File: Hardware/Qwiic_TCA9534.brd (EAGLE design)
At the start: 30.5 x 25.4 mm, 24 parts, among them J2 SMD, J3 PTH, J4 SMD

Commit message: partial route
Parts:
- removed J8: (no value), SparkFun-Connectors:1X10_NO_SILK
- added J5: (no value), SparkFun-Connectors:1X08_NO_SILK
- moved R5 19.8 mm to (6.86, 5.08), turned to 0 degrees
- moved JP7 11.7 mm to (11.4, 6.35)
- moved JP5 7.62 mm to (15.2, 6.35)
- moved JP1 4.58 mm to (19.1, 6.35)
- moved R3 3.30 mm to (23.6, 5.08)
- moved R1 3.05 mm to (23.6, 7.62)
- moved C4 0.52 mm to (6.86, 7.49)
- moved R2 0.51 mm to (12.7, 19.8)
- moved R4 0.51 mm to (17.8, 19.8)
- moved SJ5 0.38 mm to (15.2, 19.9)
- moved U$2 0.28 mm to (26.2, 20.3)
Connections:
- removed net 2: J8.3, U$3.5
- removed net SCL/SCK/RX: J2.4, J3.4, J4.4
- removed net SDA/MISO/TX: J2.3, J3.3, J4.3
- new net P1: J5.2, U$3.5
- net GND: no longer J8.1, J8.10
- net P0: now also J5.1; no longer J8.2
- net P2: now also J5.3; no longer J8.4
- net P3: now also J5.4; no longer J8.5
- net P4: now also J5.5; no longer J8.6
- net P5: now also J5.6; no longer J8.7
- net P6: now also J5.7; no longer J8.8
- net P7: now also J5.8; no longer J8.9
- net SCL: now also J2.4, J3.4, J4.4, R4.1
- net SDA: now also J2.3, J3.3, J4.3, R2.1
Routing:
- net 3.3V: track 0.00 -> 27.0 mm
- net SCL: track 0.00 -> 20.8 mm, vias 0 -> 2
- net SDA: track 0.00 -> 18.4 mm
- net !INT: track 0.00 -> 16.4 mm
- net P0: track 0.00 -> 15.5 mm
- net P1: track 0.00 -> 14.2 mm
- net P7: track 0.00 -> 13.2 mm
- net P2: track 0.00 -> 13.0 mm
- net P6: track 0.00 -> 11.9 mm
- net P3: track 0.00 -> 11.7 mm
- net P5: track 0.00 -> 10.6 mm
- net P4: track 0.00 -> 8.39 mm
- net A1: track 0.00 -> 6.58 mm
- net A2: track 0.00 -> 4.99 mm
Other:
- board text added: "Qwiic GPIO"

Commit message: route complete
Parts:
- moved R2 0.25 mm to (12.7, 19.6), turned to 90 degrees
- moved R4 0.25 mm to (17.8, 19.6), turned to 90 degrees
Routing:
- net 3.3V: track 27.0 -> 72.3 mm, vias 0 -> 4
- net A0: track 0.00 -> 33.9 mm, vias 0 -> 2
- net SDA: track 18.4 -> 46.6 mm, vias 0 -> 4
- net SCL: track 20.8 -> 43.3 mm, vias 2 -> 5
- net A1: track 6.58 -> 14.7 mm, vias 0 -> 1
- net SCL_PU1: track 0.00 -> 7.50 mm, vias 0 -> 1
- net SDA_PU1: track 0.00 -> 7.34 mm, vias 0 -> 1
- net A2: track 4.99 -> 10.0 mm, vias 0 -> 1
- net GND: track 0.00 -> 2.70 mm, vias 0 -> 2
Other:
- board text removed: "TCA9534"

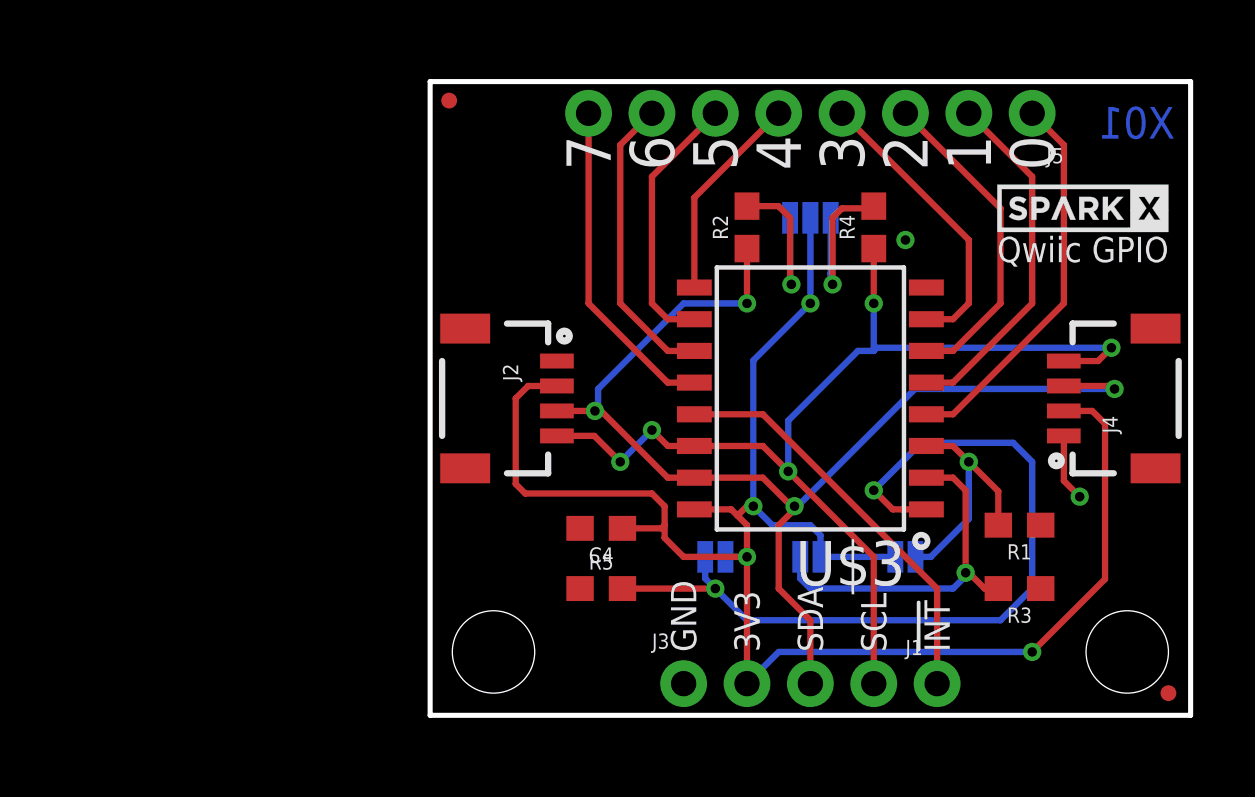
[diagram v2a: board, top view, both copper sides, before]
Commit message: starting to build out example 1
example 1 is to set a pin on the expander as output or input, then set it as high or low. currently the setPinMode() function works, next is to make a 'digitalWrite' equivalent
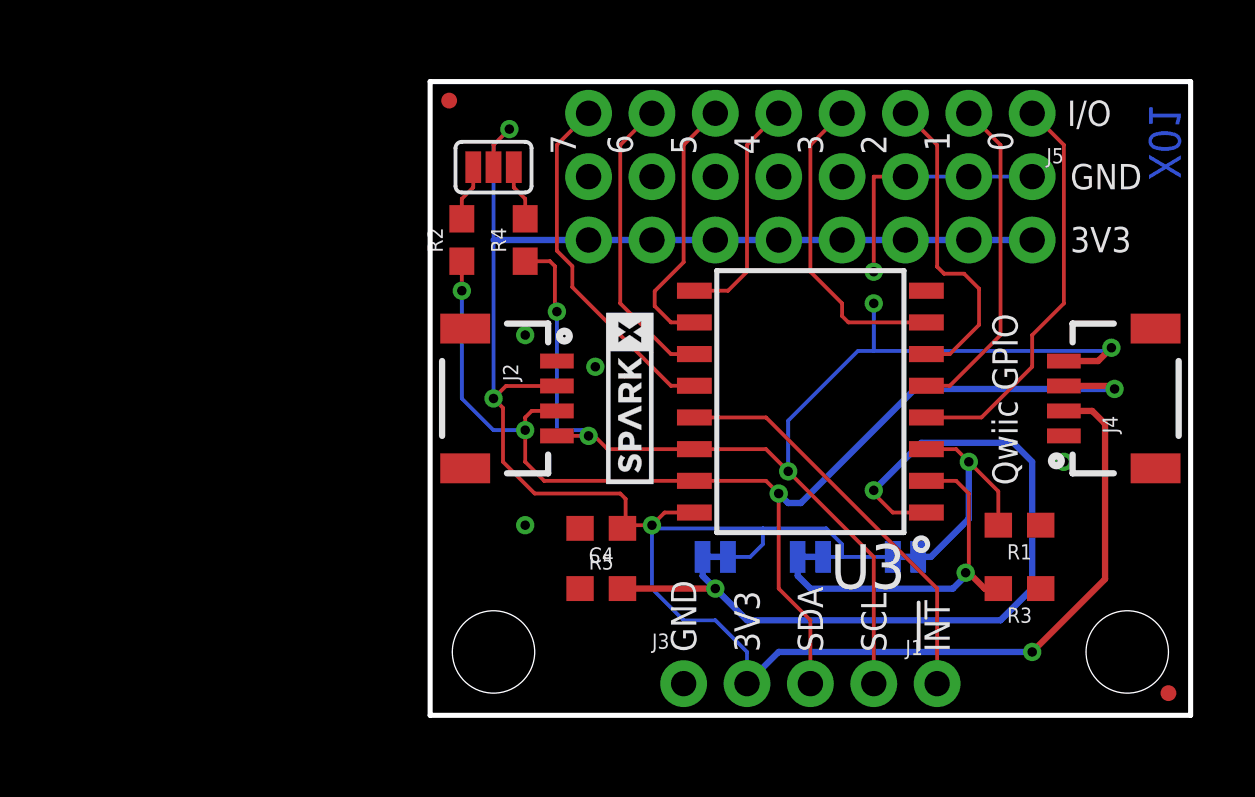
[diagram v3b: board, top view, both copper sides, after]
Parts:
- removed U$3: TCA9534U, KevinKuwata_eagle:16SOIC
- added J6, J7: (no value), SparkFun-Connectors:1X08_NO_SILK
- added U3: TCA9534U, KevinKuwata_eagle:16SOIC
- JP1, JP5, JP7: value JUMPER-SMT_2_NC_PASTE_NO-SILK -> JUMPER-SMT_2_NC_TRACE_NO-SILK; device SparkFun-Jumpers:SMT-JUMPER_2_NC_PASTE_NO-SILK -> SparkFun-Jumpers:SMT-JUMPER_2_NC_TRACE_NO-SILK
- SJ5: value (none) -> SMT-JUMPER-_3-2-NC-PASTE_TALL; device SparkFun-Jumpers:SMT-JUMPER_3_2-NC_PASTE_SILK -> KevinKuwata_eagle:SMT-JUMPER_3-2-NC-PASTE_SILK_TALLER_A
- moved U$2 19.7 mm to (8.00, 12.7), turned to 90 degrees
- moved R4 14.0 mm to (3.81, 19.1)
- moved SJ5 12.9 mm to (2.54, 22.0), flipped to the top, turned to 0 degrees
- moved R2 11.4 mm to (1.27, 19.1)
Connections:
- net !INT: now also U3.13; no longer U$3.13
- net 3.3V: now also J7.1, J7.2, J7.3, J7.4, J7.5, J7.6, J7.7, J7.8, U3.16; no longer U$3.16
- net A0: now also U3.1; no longer U$3.1
- net A1: now also U3.2; no longer U$3.2
- net A2: now also U3.3; no longer U$3.3
- net GND: now also J6.1, J6.2, J6.3, J6.4, J6.5, J6.6, J6.7, J6.8, U3.8; no longer U$3.8
- net P0: now also U3.4; no longer U$3.4
- net P1: now also U3.5; no longer U$3.5
- net P2: now also U3.6; no longer U$3.6
- net P3: now also U3.7; no longer U$3.7
- net P4: now also U3.9; no longer U$3.9
- net P5: now also U3.10; no longer U$3.10
- net P6: now also U3.11; no longer U$3.11
- net P7: now also U3.12; no longer U$3.12
- net SCL: now also U3.14; no longer U$3.14
- net SDA: now also U3.15; no longer U$3.15
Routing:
- net 3.3V: track 72.3 -> 96.4 mm
- net GND: track 2.70 -> 10.2 mm, vias 2 -> 5
- net SCL: track 43.3 -> 49.3 mm
- net SCL_PU1: track 7.50 -> 2.26 mm, vias 1 -> 0
- net SDA_PU1: track 7.34 -> 2.26 mm, vias 1 -> 0
- net SDA: track 46.6 -> 48.1 mm
- net P7: track 13.2 -> 14.3 mm
- net P1: track 14.2 -> 13.2 mm
- net P3: track 11.7 -> 12.7 mm
- net P4: track 8.39 -> 9.30 mm
- net P0: track 15.5 -> 16.3 mm
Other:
- board text added: "A0"
- board text added: "A1"
- board text added: "A2"
- board text added: "I/O"
- board text removed: "I2C ADR"
